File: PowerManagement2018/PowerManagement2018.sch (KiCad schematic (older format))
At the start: 25 parts, among them J1 Conn_01x02_Male, J2 Conn_01x02_Male, J3 Conn_01x02_Male, J4 Conn_01x02_Male, Q1 Q_PMOS_GSD

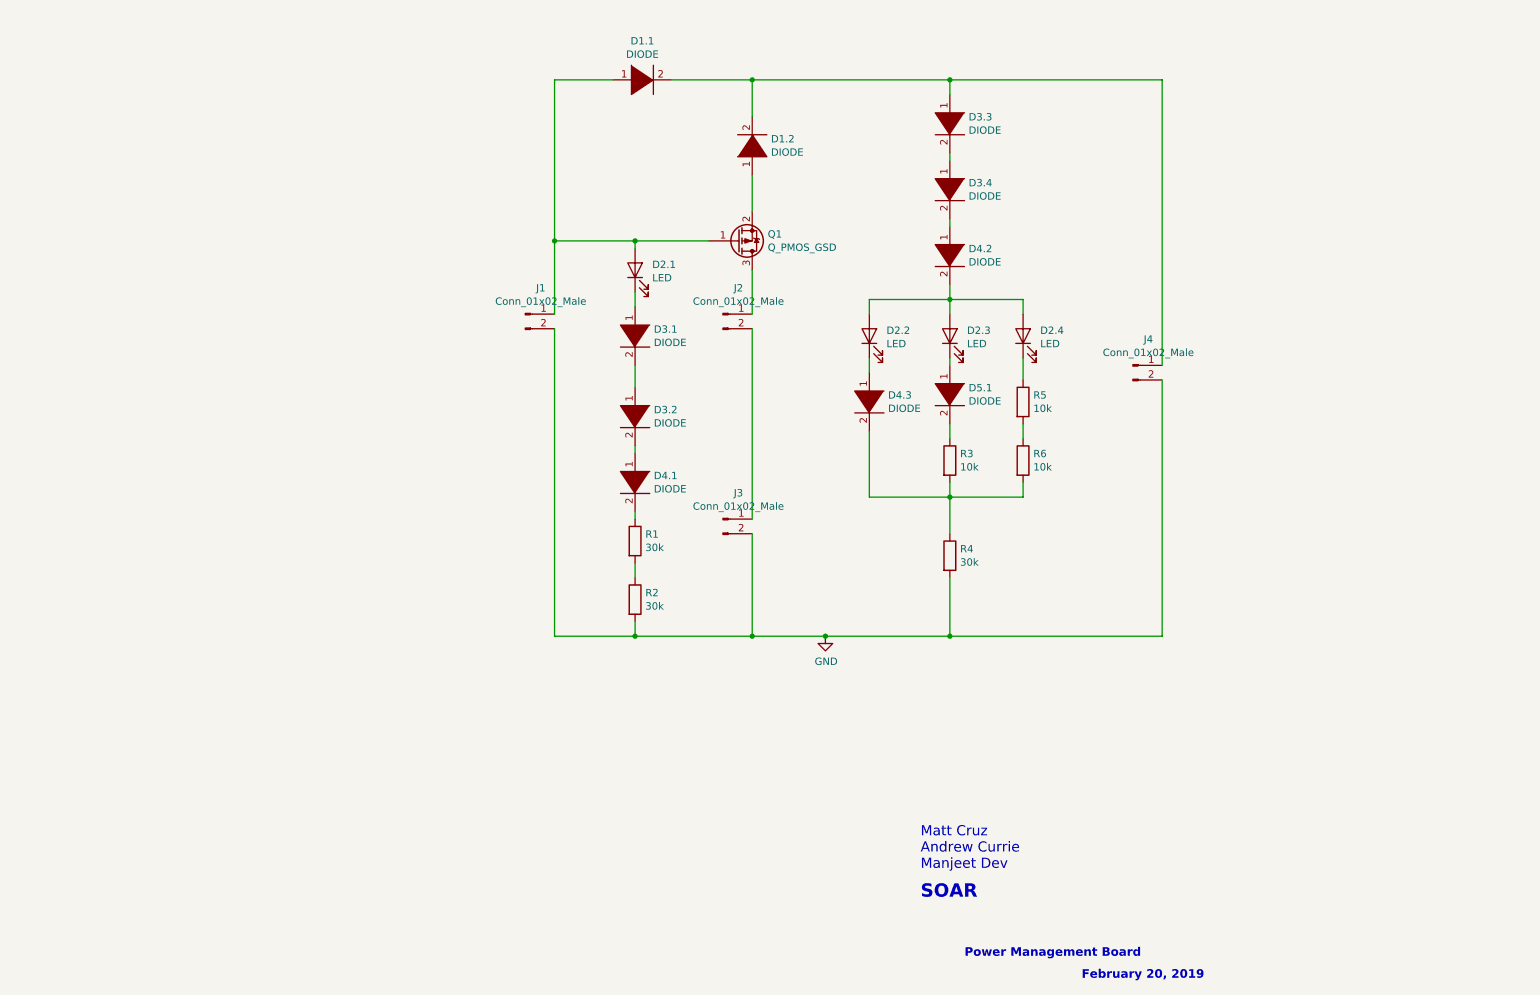
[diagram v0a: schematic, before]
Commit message: Combined system
Battery charging system and battery switching system combined
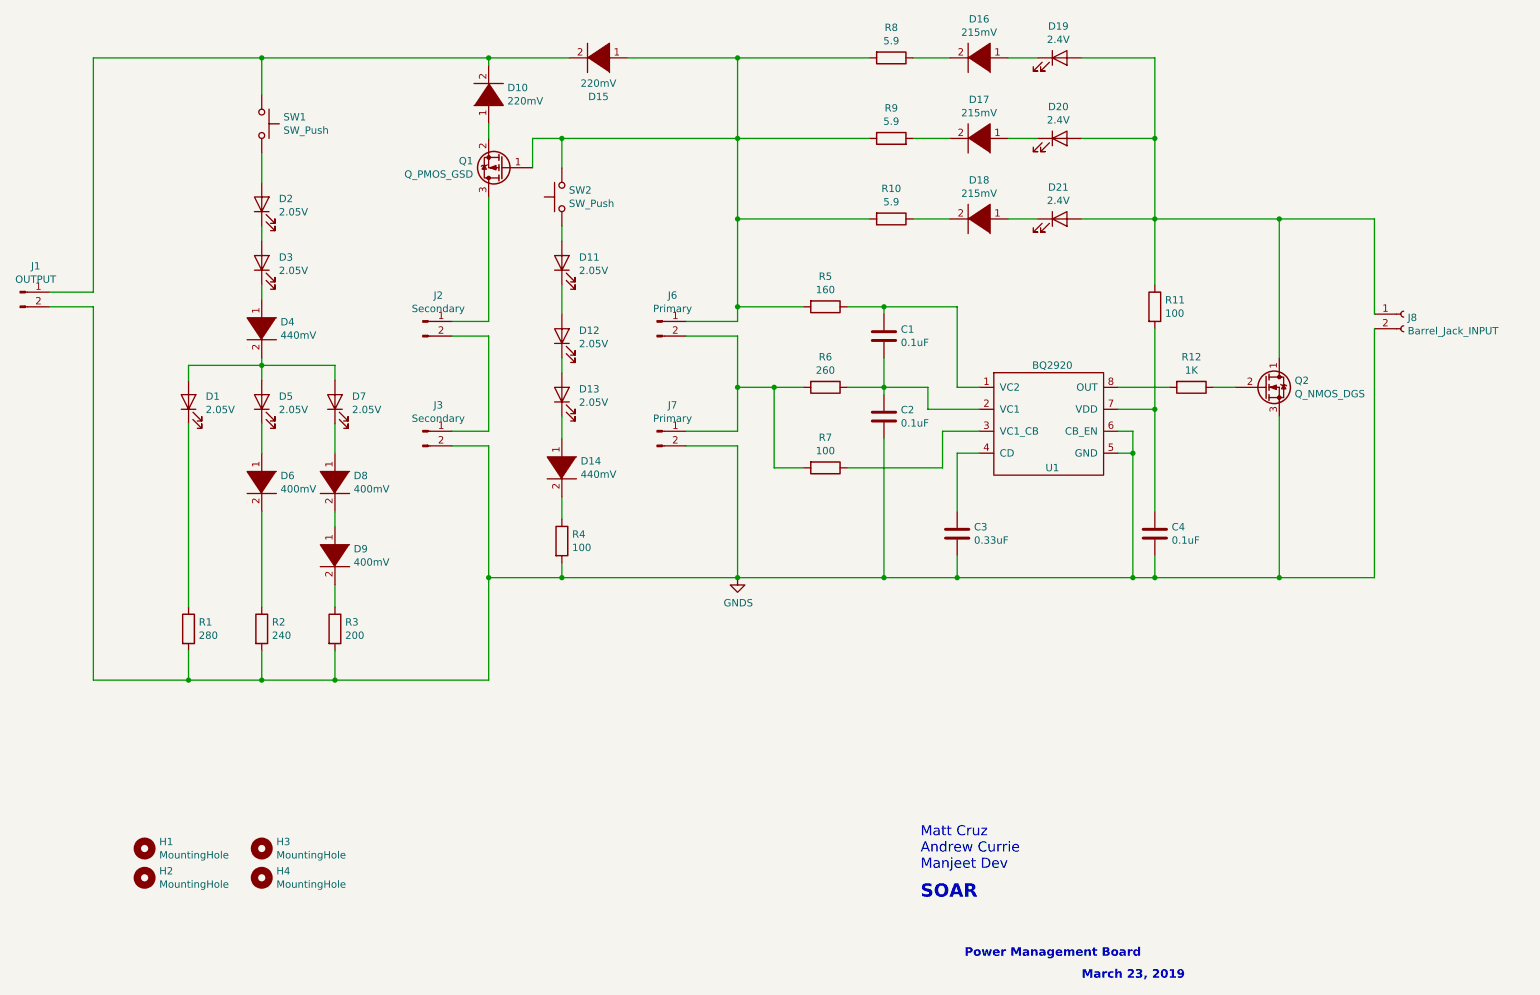
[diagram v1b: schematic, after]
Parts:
- removed D2.1, D2.2, D2.3, D2.4: LED, PowerManagementBoard:LTST-C191KFKT(LED 2V), symbol Device:LED
- removed D3.1, D3.2, D3.3, D3.4: DIODE, PowerManagementBoard:CD214A-R150_R11600(Diode 2V), symbol pspice:DIODE
- removed D4.1, D4.2, D4.3: DIODE, PowerManagementBoard:CES388(Diode 0.6V), symbol pspice:DIODE
- removed D5.1: DIODE, PowerManagementBoard:MBR120VLSF(Diode 0.3V), symbol pspice:DIODE
- removed J4: Conn_01x02_Male, SOAR_Kicad_Library-master:Molex_Micro-Fit_3.0_43045-0600_2x03_P3.00mm_Horizontal, symbol Connector:Conn_01x02_Male
- added C1, C2, C4: 0.1uF, New_Library:CL05B104KP5NNNC (0.1uF), symbol Device:C
- added C3: 0.33uF, New_Library:CL21B334KBFNNNE (0.33uF), symbol Device:C
- added D1, D5, D7: 2.05V, New_Library:SML-D12U1WT86 (2.05V 10mA), symbol Device:LED
- added D11, D12, D13, D2, D3: 2.05V, New_Library:LTST-C190KFKT (2.05V 30mA), symbol Device:LED
- added D14, D4: 440mV, New_Library:BAT42WS-7-F (0.44V 30mA), symbol pspice:DIODE
- added D16, D17, D18: 215mV, New_Library:PMEG1020EH (215mV diode), symbol pspice:DIODE
- added D19, D20, D21: 2.4V, New_Library:XZMYH160S (2.5V LED), symbol Device:LED
- added D6, D8, D9: 400mV, New_Library:BAT46W-E3-08(0.4V10mA), symbol pspice:DIODE
- added H1, H2, H3, H4: MountingHole, MountingHole:MountingHole_3mm, symbol Mechanical:MountingHole
- added J6, J7: Primary, New_Library:deans connector, symbol Connector:Conn_01x02_Male
- added J8: Barrel_Jack_INPUT, SOAR_Kicad_Library-master:CUI_PJ-102A_2.5mm_DC_JACK, symbol Connector:Conn_01x02_Female
- added Q2: Q_NMOS_DGS, New_Library:AO3414 (nmos), symbol Device:Q_NMOS_DGS
- added R10, R8, R9: 5.9, New_Library:CRCW25125R90FKEGHP(5.9 ohms), symbol Device:R
- added R11: 100, New_Library:RT0603(resistors), symbol Device:R
- added R12: 1K, New_Library:RC0201(resistors), symbol Device:R
- added R7: 100, New_Library:RC0201(resistors), symbol Device:R
- added SW1, SW2: SW_Push, New_Library:1301.9320 (button), symbol Switch:SW_Push
- added U1: BQ2920, New_Library:bq29209, symbol New_Library:BQ2920
- D10: renamed from D1.2; value DIODE -> 220mV; footprint PowerManagementBoard:UPS115U (Diode 0.22V) -> New_Library:UPS115U (Diode 0.22V)
- D15: renamed from D1.1; value DIODE -> 220mV; footprint PowerManagementBoard:UPS115U (Diode 0.22V) -> New_Library:UPS115U (Diode 0.22V)
- J1: value Conn_01x02_Male -> OUTPUT; footprint PowerManagementBoard:deans connector -> SOAR_Kicad_Library-master:Molex_Micro-Fit_3.0_43045-0400_2x02_P3.00mm_Horizontal
- J2, J3: value Conn_01x02_Male -> Secondary; footprint PowerManagementBoard:deans connector -> New_Library:deans connector
- R1: value 30k -> 280; footprint PowerManagementBoard:RT0603DRD0730KL(30K resistors) -> New_Library:RC0402(resistors)
- R2: value 30k -> 240; footprint PowerManagementBoard:RT0603DRD0730KL(30K resistors) -> New_Library:RC0402(resistors)
- R3: value 10k -> 200; footprint PowerManagementBoard:RMCF0201(resistor 10k) -> New_Library:RC0201(resistors)
- R4: value 30k -> 100; footprint PowerManagementBoard:RT0603DRD0730KL(30K resistors) -> New_Library:RC0201(resistors)
- R5: value 10k -> 160; footprint PowerManagementBoard:RMCF0201(resistor 10k) -> New_Library:RC0402(resistors)
- R6: value 10k -> 260; footprint PowerManagementBoard:RMCF0201(resistor 10k) -> New_Library:RC0402(resistors)
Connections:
- net at D15.1 (K), Q1.1 (G): now also R5.2, J6.1 (Pin_1), R10.2, R8.2, R9.1, SW2.2; no longer J1.1 (Pin_1)
- net at D10.2 (A), D15.2 (A): now also J1.1 (Pin_1), SW1.1
- net at R5.1: now also C1.1, U1.1 (VC2)
- net at R3.1: now also D9.2 (A)
- net at R6.1: now also C1.2, C2.1, U1.2 (VC1); no longer R5.2
- net at R2.1: now also D6.2 (A); no longer R1.2
- net at R1.1: now also D1.1 (K)
- net GND renamed GNDS
- net GNDS: now also R1.2, R3.2, C2.2, C3.2, C4.2, J7.2 (Pin_2), J8.2 (Pin_2), Q2.3 (S), U1.5 (GND), U1.6 (CB_EN)
- new net: R7.1, U1.3 (VC1_CB)
- new net: C3.1, U1.4 (CD)
- new net: C4.1, R11.2, U1.7 (VDD)
- new net: R12.2, U1.8 (OUT)
- new net: Q2.2 (G), R12.1
- new net: D19.2 (A), D20.2 (A), D21.2 (A), J8.1 (Pin_1), Q2.1 (D), R11.1
- new net: J6.2 (Pin_2), J7.1 (Pin_1), R6.2, R7.2
- new net: D3.1 (K), D4.1 (K)
- new net: D1.2 (A), D4.2 (A), D5.2 (A), D7.2 (A)
- new net: D2.1 (K), D3.2 (A)
- new net: D2.2 (A), SW1.2
- new net: D5.1 (K), D6.1 (K)
- new net: D7.1 (K), D8.1 (K)
- new net: D8.2 (A), D9.1 (K)
- new net: D16.1 (K), D19.1 (K)
- new net: D17.1 (K), D20.1 (K)
- new net: D18.1 (K), D21.1 (K)
- new net: D16.2 (A), R8.1
- new net: D17.2 (A), R9.2
- new net: D18.2 (A), R10.1
- new net: D12.1 (K), D13.2 (A)
- new net: D11.1 (K), D12.2 (A)
- new net: D13.1 (K), D14.1 (K)
- new net: D11.2 (A), SW2.1
- new net: D14.2 (A), R4.1
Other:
- note added: "March 23, 2019"
- note removed: "February 20, 2019"
- moved on the sheet: D10, D15, J2, J3, Q1
